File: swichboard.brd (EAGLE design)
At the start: 60 x 50 mm, 9 parts, among them X1 D-SUB9-H3M09RA

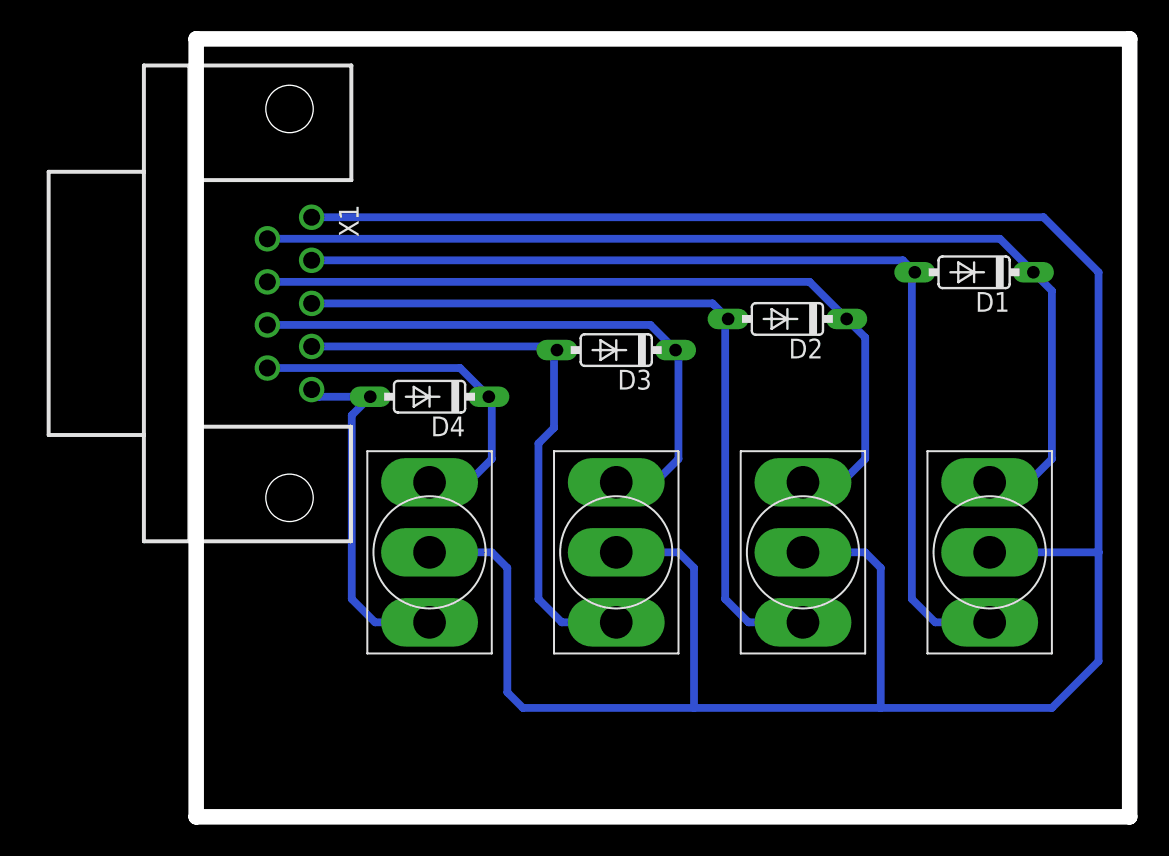
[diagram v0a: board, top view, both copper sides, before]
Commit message: add text/drillholes/copper fill to swichboard
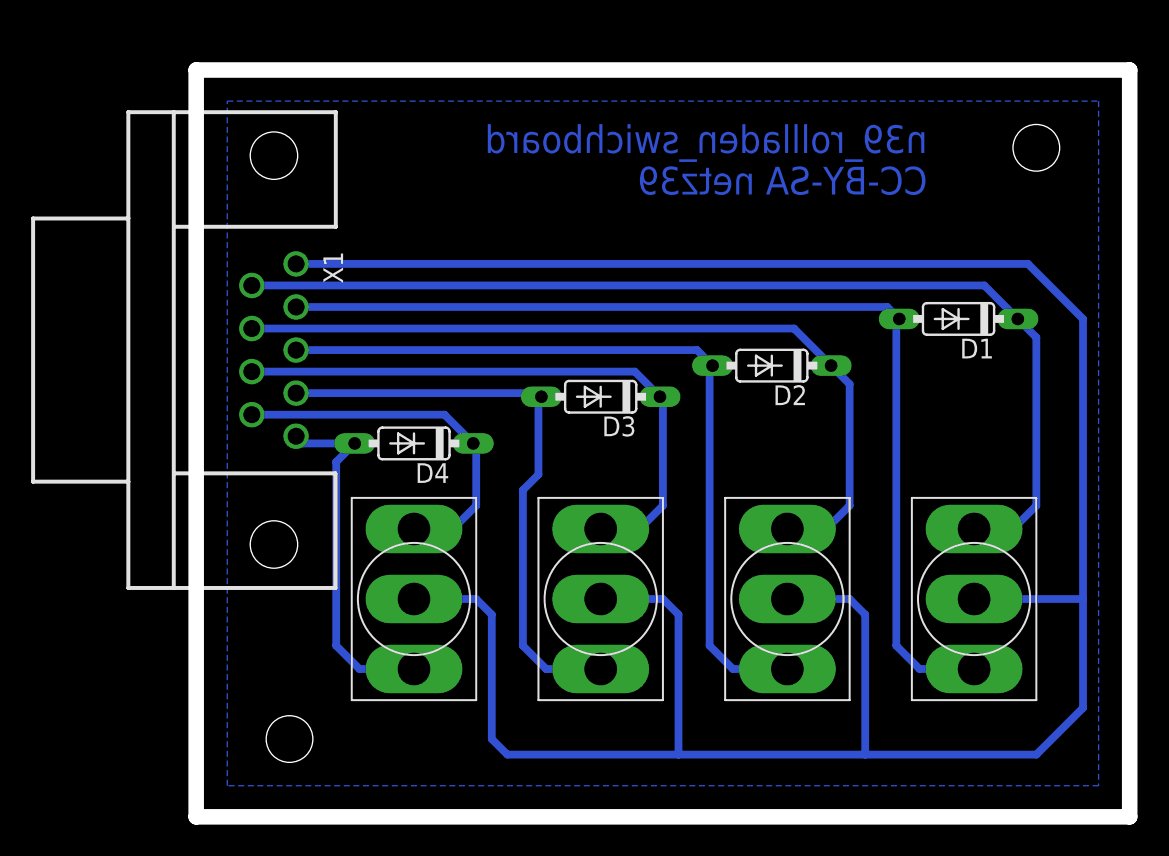
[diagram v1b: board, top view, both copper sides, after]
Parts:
- moved D1 3.16 mm to (49.0, 32.0)
- moved D2 3.16 mm to (37.0, 29.0)
- moved D3 3.16 mm to (26.0, 27.0)
- moved D4 3.16 mm to (14.0, 24.0)
- moved U$1 3.16 mm to (50.0, 14.0)
- moved U$2 3.16 mm to (38.0, 14.0)
- moved U$3 3.16 mm to (26.0, 14.0)
- moved U$4 3.16 mm to (14.0, 14.0)
- moved X1 3.16 mm to (5.00, 30.0)
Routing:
- added copper zone on layer 16, net GND
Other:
- board size 60 x 50 mm -> 60 x 48 mm
- board text added: "n39_rollladen_swichboard CC-BY-SA netz39"
